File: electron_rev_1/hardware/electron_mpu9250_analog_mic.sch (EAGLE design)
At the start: 43 parts, among them IC2 S25FL128SAGNFI011, IC4 MIC_I2S_SPH0645, U1 MPU-9250, U10 GAS_SENSOR, U2 Value, U3 OPA322AIDBVT, U4 microSD, U5 +12v, U6 +12v, U7 GAS_SENSOR

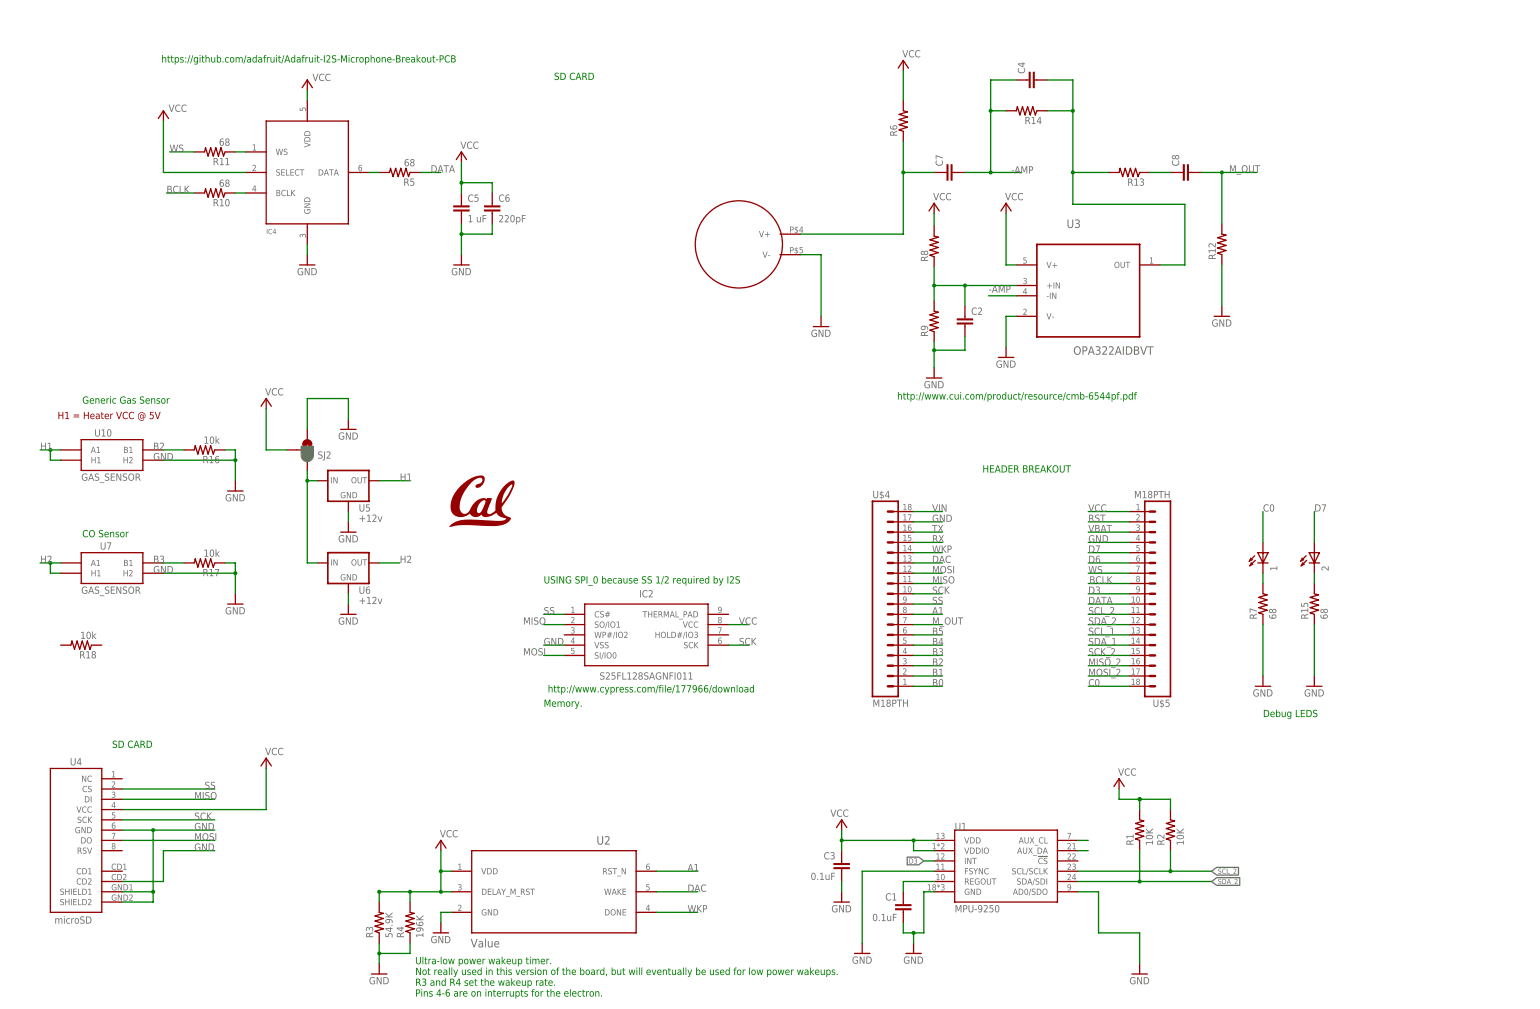
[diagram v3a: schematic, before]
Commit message: gas sensors powered from battery now
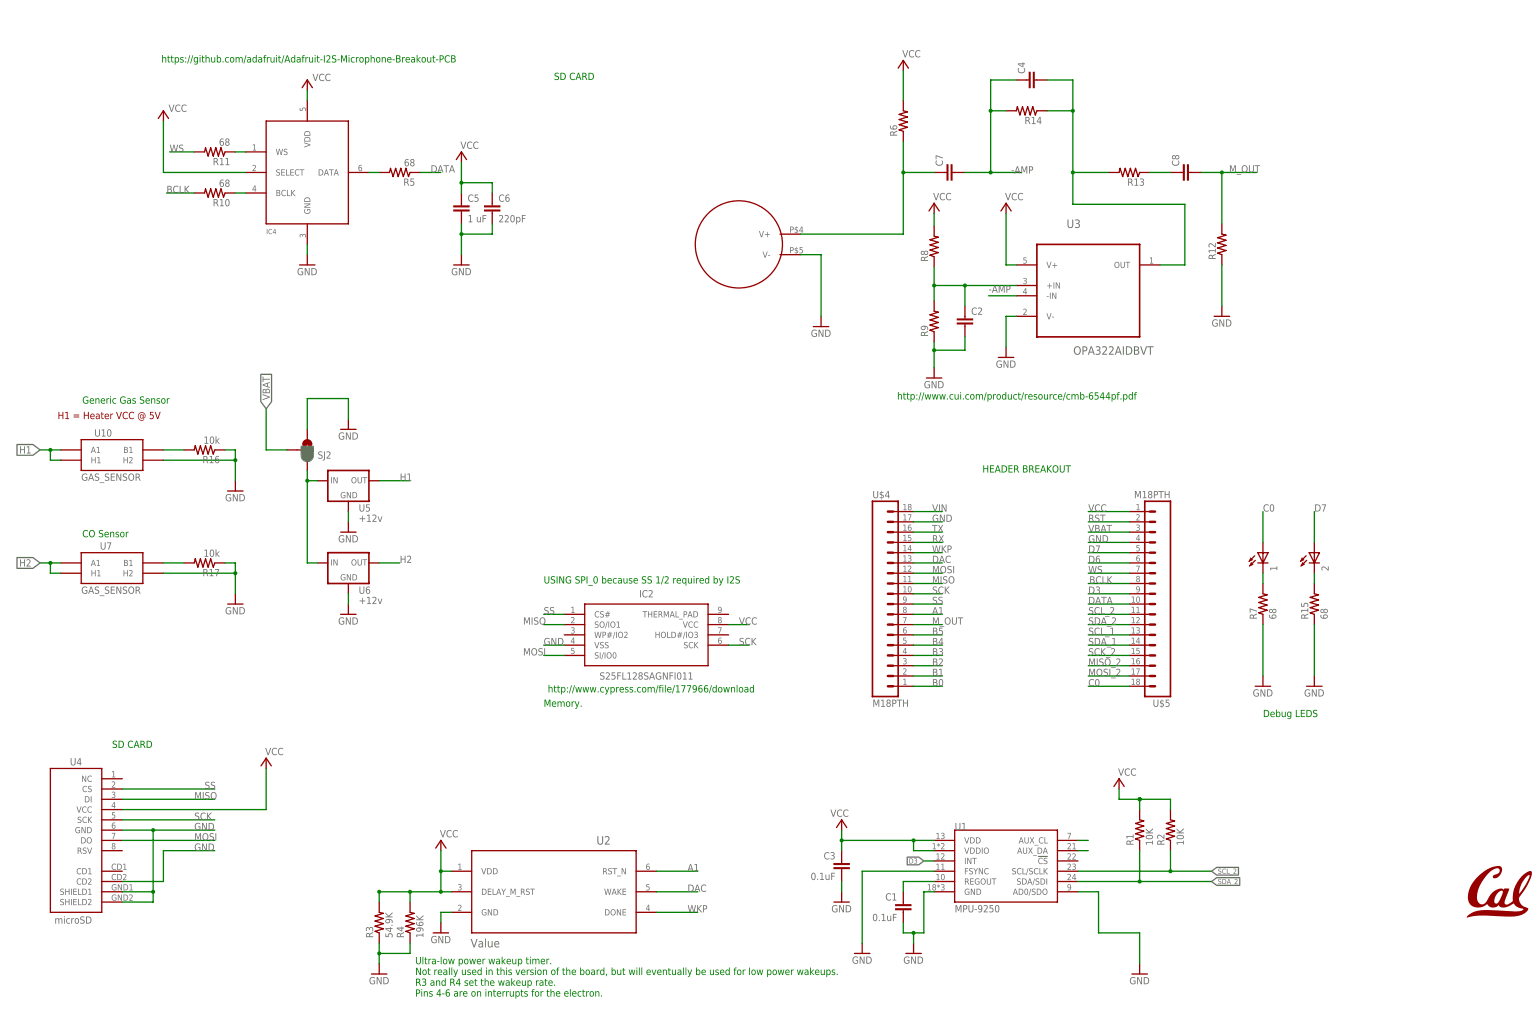
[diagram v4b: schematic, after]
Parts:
- removed R18: 10k, resistor:R-US_R0603
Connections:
- net VBAT: now also SJ2.2
- net VCC: no longer SJ2.2
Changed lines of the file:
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@@
 <part name="GND17" library="SparkFun-Aesthetics" deviceset="GND" device=""/>
 <part name="GND18" library="SparkFun-Aesthetics" deviceset="GND" device=""/>
-<part name="P+7" library="supply1" library_urn="urn:adsk.eagle:library:371" deviceset="VCC" device=""/>
 <part name="SJ2" library="SparkFun-Passives" deviceset="JUMPER_PAD-3-1&amp;2_NC_BY_PASTE" device=""/>
 <part name="GND19" library="supply1" library_urn="urn:adsk.eagle:library:371" deviceset="GND" device=""/>
 <part name="L1" library="logos" deviceset="UCB_CAL" device="100MIL"/>
-<part name="R18" library="resistor" library_urn="urn:adsk.eagle:library:348" deviceset="R-US_" device="R0603" package3d_urn="urn:adsk.eagle:package:26057/1" value="10k"/>
 </parts>
 <sheets>
@@
 <instance part="GND17" gate="1" x="-15.24" y="68.58"/>
 <instance part="GND18" gate="1" x="-15.24" y="88.9"/>
-<instance part="P+7" gate="VCC" x="-35.56" y="121.92" smashed="yes">
-<attribute name="VALUE" x="-35.814" y="122.682" size="1.778" layer="96"/>
-</instance>
 <instance part="SJ2" gate="G$1" x="-25.4" y="109.22" smashed="yes" rot="MR180">
 <attribute name="NAME" x="-22.86" y="108.839" size="1.778" layer="95" rot="MR180"/>
 </instance>
 <instance part="GND19" gate="1" x="-15.24" y="114.3"/>
-<instance part="L1" gate="G$1" x="17.78" y="96.52"/>
-<instance part="R18" gate="G$1" x="-81.28" y="60.96" rot="R180"/>
+<instance part="L1" gate="G$1" x="269.24" y="0"/>
 </instances>
 <busses>
@@
 <wire x1="-43.18" y1="109.22" x2="-43.18" y2="106.68" width="0.1524" layer="91"/>
 <wire x1="-43.18" y1="106.68" x2="-43.18" y2="101.6" width="0.1524" layer="91"/>
-<label x="-63.5" y="106.68" size="1.778" layer="95"/>
 <pinref part="U10" gate="G$1" pin="H2"/>
 <wire x1="-60.96" y1="106.68" x2="-43.18" y2="106.68" width="0.1524" layer="91"/>
@@
 <wire x1="-43.18" y1="81.28" x2="-43.18" y2="78.74" width="0.1524" layer="91"/>
 <wire x1="-43.18" y1="78.74" x2="-43.18" y2="73.66" width="0.1524" layer="91"/>
-<label x="-63.5" y="78.74" size="1.778" layer="95"/>
 <pinref part="U7" gate="G$1" pin="H2"/>
 <wire x1="-60.96" y1="78.74" x2="-43.18" y2="78.74" width="0.1524" layer="91"/>
@@
 </segment>
 <segment>
-<label x="-63.5" y="81.28" size="1.778" layer="95"/>
 <pinref part="U7" gate="G$1" pin="B1"/>
 <pinref part="R17" gate="G$1" pin="2"/>
@@
 </segment>
 <segment>
-<label x="-63.5" y="109.22" size="1.778" layer="95"/>
 <pinref part="U10" gate="G$1" pin="B1"/>
 <pinref part="R16" gate="G$1" pin="2"/>
@@
 <wire x1="177.8" y1="88.9" x2="167.64" y2="88.9" width="0.1524" layer="91"/>
 <label x="167.64" y="88.9" size="1.778" layer="95"/>
+</segment>
+<segment>
+<pinref part="SJ2" gate="G$1" pin="2"/>
+<wire x1="-30.48" y1="109.22" x2="-35.56" y2="109.22" width="0.1524" layer="91"/>
+<wire x1="-35.56" y1="109.22" x2="-35.56" y2="119.38" width="0.1524" layer="91"/>
+<label x="-35.56" y="119.38" size="1.778" layer="95" rot="R90" xref="yes"/>
 </segment>
 </net>
@@
 <wire x1="-35.56" y1="20.32" x2="-35.56" y2="30.48" width="0.1524" layer="91"/>
 </segment>
-<segment>
-<pinref part="SJ2" gate="G$1" pin="2"/>
-<wire x1="-30.48" y1="109.22" x2="-35.56" y2="109.22" width="0.1524" layer="91"/>
-<pinref part="P+7" gate="VCC" pin="VCC"/>
-<wire x1="-35.56" y1="109.22" x2="-35.56" y2="119.38" width="0.1524" layer="91"/>
-</segment>
 </net>
 <net name="SCL_1" class="0">
@@
 <pinref part="U10" gate="G$1" pin="H1"/>
 <wire x1="-88.9" y1="109.22" x2="-86.36" y2="109.22" width="0.1524" layer="91"/>
-<label x="-91.44" y="109.22" size="1.778" layer="95"/>
 <pinref part="U10" gate="G$1" pin="A1"/>
 <wire x1="-88.9" y1="106.68" x2="-88.9" y2="109.22" width="0.1524" layer="91"/>
 <wire x1="-88.9" y1="109.22" x2="-91.44" y2="109.22" width="0.1524" layer="91"/>
 <junction x="-88.9" y="109.22"/>
+<label x="-91.44" y="109.22" size="1.778" layer="95" rot="R180" xref="yes"/>
 </segment>
 <segment>
@@
 <pinref part="U7" gate="G$1" pin="H1"/>
 <wire x1="-88.9" y1="81.28" x2="-86.36" y2="81.28" width="0.1524" layer="91"/>
-<label x="-91.44" y="81.28" size="1.778" layer="95"/>
 <pinref part="U7" gate="G$1" pin="A1"/>
 <wire x1="-88.9" y1="78.74" x2="-88.9" y2="81.28" width="0.1524" layer="91"/>
 <wire x1="-88.9" y1="81.28" x2="-91.44" y2="81.28" width="0.1524" layer="91"/>
 <junction x="-88.9" y="81.28"/>
-</segment>
-<segment>
+<label x="-91.44" y="81.28" size="1.778" layer="95" rot="R180" xref="yes"/>
+</segment>
+<segment>

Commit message: fixed stupid error with solder jumper...
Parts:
- removed SJ2: JUMPER_PAD-3-1&2_NC_BY_PASTE, SparkFun-Passives:JUMPER_PAD-3-1&2_NC_BY_PASTE
- added SJ1: (no value), jumper:SJ
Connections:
- net GND: no longer SJ2.3
- net N$10: now also SJ1.1; no longer SJ2.1
- net VBAT: now also SJ1.2; no longer SJ2.2
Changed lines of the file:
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@@
 <part name="GND17" library="SparkFun-Aesthetics" deviceset="GND" device=""/>
 <part name="GND18" library="SparkFun-Aesthetics" deviceset="GND" device=""/>
-<part name="SJ2" library="SparkFun-Passives" deviceset="JUMPER_PAD-3-1&amp;2_NC_BY_PASTE" device=""/>
-<part name="GND19" library="supply1" library_urn="urn:adsk.eagle:library:371" deviceset="GND" device=""/>
 <part name="L1" library="logos" deviceset="UCB_CAL" device="100MIL"/>
+<part name="SJ1" library="jumper" library_urn="urn:adsk.eagle:library:252" deviceset="SJ" device="" package3d_urn="urn:adsk.eagle:package:15471/1"/>
 </parts>
 <sheets>
@@
 <instance part="GND17" gate="1" x="-15.24" y="68.58"/>
 <instance part="GND18" gate="1" x="-15.24" y="88.9"/>
-<instance part="SJ2" gate="G$1" x="-25.4" y="109.22" smashed="yes" rot="MR180">
-<attribute name="NAME" x="-22.86" y="108.839" size="1.778" layer="95" rot="MR180"/>
-</instance>
-<instance part="GND19" gate="1" x="-15.24" y="114.3"/>
 <instance part="L1" gate="G$1" x="269.24" y="0"/>
+<instance part="SJ1" gate="1" x="-25.4" y="109.22" rot="R90"/>
 </instances>
 <busses>
@@
 <wire x1="-15.24" y1="73.66" x2="-15.24" y2="71.12" width="0.1524" layer="91"/>
 </segment>
-<segment>
-<pinref part="GND19" gate="1" pin="GND"/>
-<wire x1="-15.24" y1="116.84" x2="-15.24" y2="121.92" width="0.1524" layer="91"/>
-<pinref part="SJ2" gate="G$1" pin="3"/>
-<wire x1="-25.4" y1="114.3" x2="-25.4" y2="121.92" width="0.1524" layer="91"/>
-<wire x1="-15.24" y1="121.92" x2="-25.4" y2="121.92" width="0.1524" layer="91"/>
-</segment>
 </net>
 <net name="TX" class="0">
@@
 </segment>
 <segment>
-<pinref part="SJ2" gate="G$1" pin="2"/>
-<wire x1="-30.48" y1="109.22" x2="-35.56" y2="109.22" width="0.1524" layer="91"/>
-<wire x1="-35.56" y1="109.22" x2="-35.56" y2="119.38" width="0.1524" layer="91"/>
-<label x="-35.56" y="119.38" size="1.778" layer="95" rot="R90" xref="yes"/>
+<wire x1="-25.4" y1="114.3" x2="-25.4" y2="119.38" width="0.1524" layer="91"/>
+<label x="-25.4" y="119.38" size="1.778" layer="95" rot="R90" xref="yes"/>
+<pinref part="SJ1" gate="1" pin="2"/>
 </segment>
 </net>
@@
 <pinref part="U5" gate="G$1" pin="IN"/>
 <wire x1="-22.86" y1="101.6" x2="-25.4" y2="101.6" width="0.1524" layer="91"/>
+<pinref part="SJ1" gate="1" pin="1"/>
 <wire x1="-25.4" y1="101.6" x2="-25.4" y2="104.14" width="0.1524" layer="91"/>
 <junction x="-25.4" y="101.6"/>
-<pinref part="SJ2" gate="G$1" pin="1"/>
-</segment>
-</net>
+</segment>
+</net>

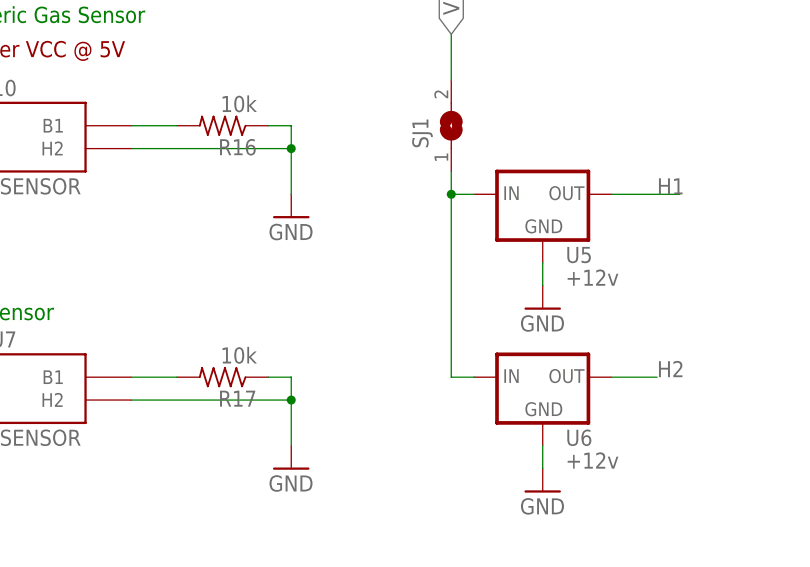
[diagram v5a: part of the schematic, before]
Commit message: seperate solder jumpers for gas sensors
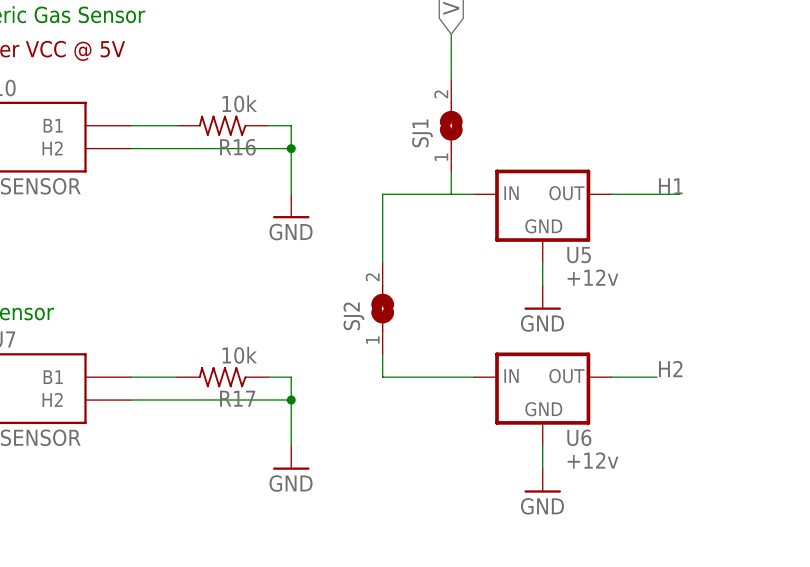
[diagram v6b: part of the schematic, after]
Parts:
- added SJ2: (no value), jumper:SJ
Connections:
- removed net N$10: SJ1.1, U5.IN, U6.IN
- new net N$11: SJ2.1, U6.IN
- net VBAT: now also SJ1.1, SJ2.2, U5.IN
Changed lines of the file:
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@@
 <part name="L1" library="logos" deviceset="UCB_CAL" device="100MIL"/>
 <part name="SJ1" library="jumper" library_urn="urn:adsk.eagle:library:252" deviceset="SJ" device="" package3d_urn="urn:adsk.eagle:package:15471/1"/>
+<part name="SJ2" library="jumper" library_urn="urn:adsk.eagle:library:252" deviceset="SJ" device="" package3d_urn="urn:adsk.eagle:package:15471/1"/>
 </parts>
 <sheets>
@@
 <instance part="L1" gate="G$1" x="269.24" y="0"/>
 <instance part="SJ1" gate="1" x="-25.4" y="109.22" rot="R90"/>
+<instance part="SJ2" gate="1" x="-33.02" y="88.9" rot="R90"/>
 </instances>
 <busses>
@@
 <label x="-25.4" y="119.38" size="1.778" layer="95" rot="R90" xref="yes"/>
 <pinref part="SJ1" gate="1" pin="2"/>
+</segment>
+<segment>
+<wire x1="-33.02" y1="93.98" x2="-33.02" y2="101.6" width="0.1524" layer="91"/>
+<pinref part="SJ2" gate="1" pin="2"/>
+<pinref part="U5" gate="G$1" pin="IN"/>
+<wire x1="-22.86" y1="101.6" x2="-25.4" y2="101.6" width="0.1524" layer="91"/>
+<pinref part="SJ1" gate="1" pin="1"/>
+<wire x1="-25.4" y1="101.6" x2="-25.4" y2="104.14" width="0.1524" layer="91"/>
+<wire x1="-33.02" y1="101.6" x2="-25.4" y2="101.6" width="0.1524" layer="91"/>
 </segment>
 </net>
@@
 </segment>
 </net>
-<net name="N$10" class="0">
+<net name="N$11" class="0">
 <segment>
 <pinref part="U6" gate="G$1" pin="IN"/>
-<wire x1="-22.86" y1="81.28" x2="-25.4" y2="81.28" width="0.1524" layer="91"/>
-<wire x1="-25.4" y1="81.28" x2="-25.4" y2="101.6" width="0.1524" layer="91"/>
-<pinref part="U5" gate="G$1" pin="IN"/>
-<wire x1="-22.86" y1="101.6" x2="-25.4" y2="101.6" width="0.1524" layer="91"/>
-<pinref part="SJ1" gate="1" pin="1"/>
-<wire x1="-25.4" y1="101.6" x2="-25.4" y2="104.14" width="0.1524" layer="91"/>
-<junction x="-25.4" y="101.6"/>
-</segment>
-</net>
+<pinref part="SJ2" gate="1" pin="1"/>
+<wire x1="-22.86" y1="81.28" x2="-33.02" y2="81.28" width="0.1524" layer="91"/>
+<wire x1="-33.02" y1="81.28" x2="-33.02" y2="83.82" width="0.1524" layer="91"/>
+</segment>
+</net>
